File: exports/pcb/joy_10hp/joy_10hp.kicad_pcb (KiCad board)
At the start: 2 copper layers, 50.8 x 128.5 mm, 1 part

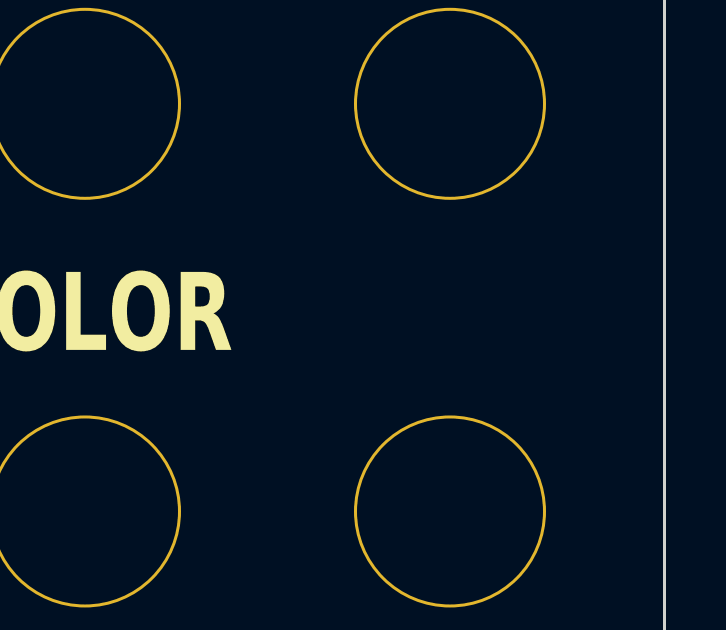
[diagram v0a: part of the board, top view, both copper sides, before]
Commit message: Regenerate Joy 10HP PCB faceplate with the FM label
daisy_braids.py now labels CV_8 "FM", so the board, gerbers and preview are
replotted from it. The only geometry change is the added F.Silkscreen text at
(43.65, 105.31); every other gerber differs solely in its date/version header
(replotted with kicad-cli 9.0.7 rather than 7.0.11). The deterministic UUIDs in
the .kicad_pcb shift by one from the extra text element.

Also documents the plot command behind preview.png, which was previously
undocumented and had to be reverse-engineered from the image's layer colours.

Co-Authored-By: Claude Opus 5 (1M context) <noreply@anthropic.com>
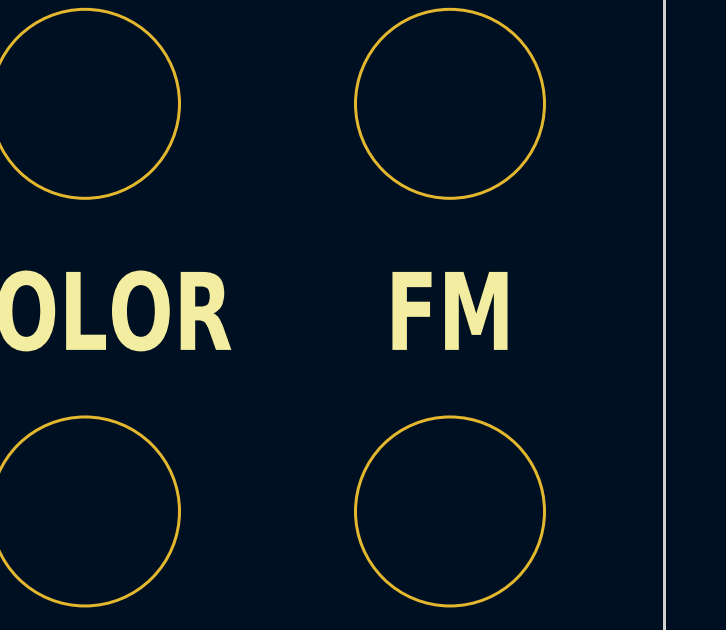
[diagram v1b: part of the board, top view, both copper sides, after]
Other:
- board text added: "FM"
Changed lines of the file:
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@@
+		(effects (font (size 2.6 1.872) (thickness 0.442) bold))
+	)
+	(gr_text "FM" (at 43.65 105.311904) (layer "F.SilkS")
 		(effects (font (size 2.6 1.872) (thickness 0.442) bold))
 	)
